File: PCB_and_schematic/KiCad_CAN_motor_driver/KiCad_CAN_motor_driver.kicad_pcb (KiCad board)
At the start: 2 copper layers, 90.4 x 45.2 mm, 67 parts, among them J1 SWDIO, J2 UART, J3 POWER IN 24V, J4 MOTOR OUT, J5 CAN, J6 PWM IN, Q1 BTN8982TA, Q2 BTN8982TA, U1 SN65HVD232, U2 LMR50410, U3 STM32F103C8Tx

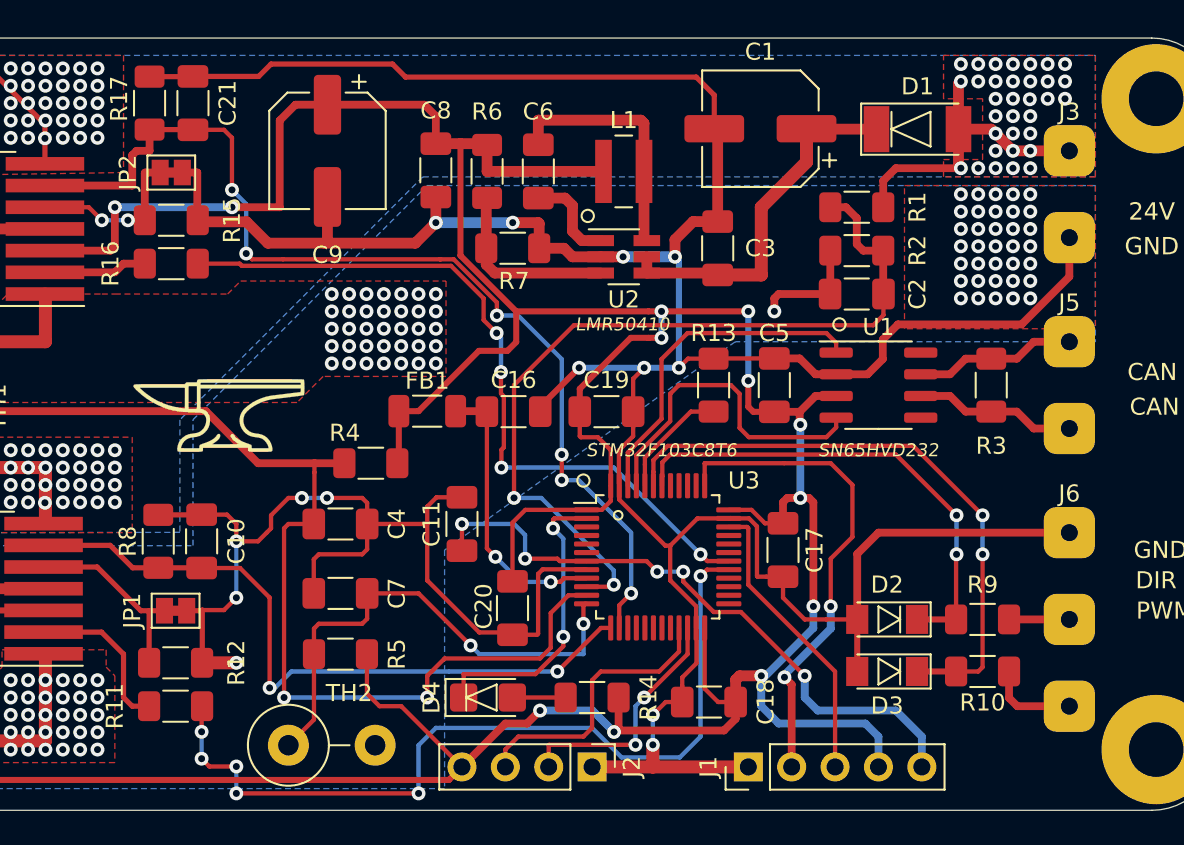
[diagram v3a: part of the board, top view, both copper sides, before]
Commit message: Added JLC PCB ID placeholder,
+traces optimization
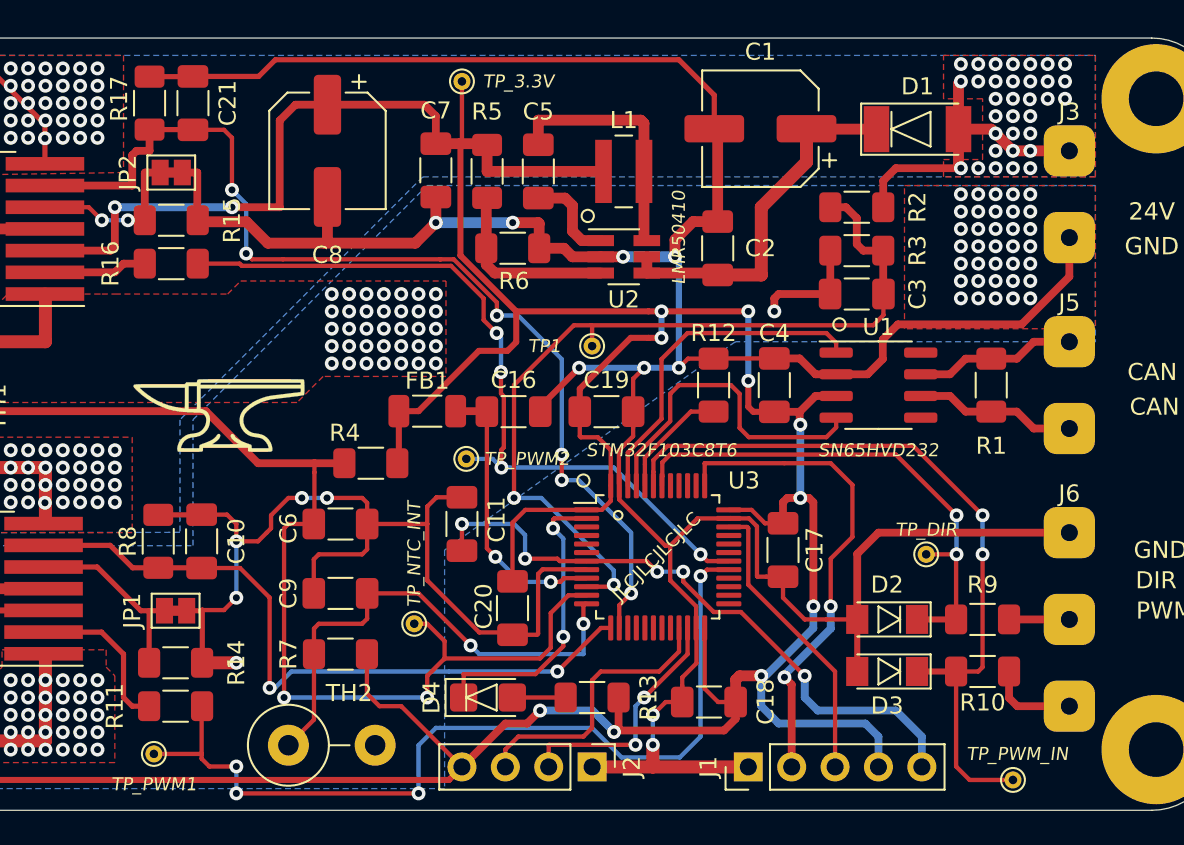
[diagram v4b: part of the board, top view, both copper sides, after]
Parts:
- added TP1: VIN, TestPoint:TestPoint_THTPad_D1.0mm_Drill0.5mm, F.Cu at (159.8, 95.0)
- added TP_3.3V: 3V3, TestPoint:TestPoint_THTPad_D1.0mm_Drill0.5mm, F.Cu at (152.1, 79.5)
- added TP_DIR: DIR, TestPoint:TestPoint_THTPad_D1.0mm_Drill0.5mm, F.Cu at (179.3, 107.2)
- added TP_NTC_INT: NTC INT, TestPoint:TestPoint_THTPad_D1.0mm_Drill0.5mm, F.Cu at (149.4, 111.3)
- added TP_PWM1: PWM OUT 1, TestPoint:TestPoint_THTPad_D1.0mm_Drill0.5mm, F.Cu at (134.1, 118.9)
- added TP_PWM2: PWM OUT 2, TestPoint:TestPoint_THTPad_D1.0mm_Drill0.5mm, F.Cu at (152.4, 101.6)
- added TP_PWM_IN: PWM IN, TestPoint:TestPoint_THTPad_D1.0mm_Drill0.5mm, F.Cu at (184.4, 120.4)
- R10, R9: value 1k -> 6.8k
- renumbered C3 to C2, C2 to C3, C5 to C4, C6 to C5, C4 to C6, C8 to C7, C9 to C8, C7 to C9, R3 to R1, R13 to R12, R14 to R13, R12 to R14, R1 to R2, R2 to R3, R6 to R5, R7 to R6, R5 to R7
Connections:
- U1 pad 5: (no net) -> Net-(U1-Pad5)
- U1 pad 8: (no net) -> Net-(U1-Pad8)
- U3 pad 15: (no net) -> Net-(U3-Pad15)
- U3 pad 16: (no net) -> Net-(U3-Pad16)
- U3 pad 17: (no net) -> Net-(U3-Pad17)
- U3 pad 18: (no net) -> Net-(U3-Pad18)
- U3 pad 19: (no net) -> Net-(U3-Pad19)
- U3 pad 20: (no net) -> Net-(U3-Pad20)
- U3 pad 25: (no net) -> Net-(U3-Pad25)
- U3 pad 26: (no net) -> Net-(U3-Pad26)
- U3 pad 27: (no net) -> Net-(U3-Pad27)
- U3 pad 28: (no net) -> Net-(U3-Pad28)
- U3 pad 3: (no net) -> Net-(U3-Pad3)
- U3 pad 31: (no net) -> Net-(U3-Pad31)
- U3 pad 32: (no net) -> Net-(U3-Pad32)
- U3 pad 33: (no net) -> Net-(U3-Pad33)
- U3 pad 38: (no net) -> Net-(U3-Pad38)
- U3 pad 39: (no net) -> Net-(U3-Pad39)
- U3 pad 4: (no net) -> Net-(U3-Pad4)
- U3 pad 40: (no net) -> Net-(U3-Pad40)
- U3 pad 41: (no net) -> Net-(U3-Pad41)
- U3 pad 5: (no net) -> Net-(U3-Pad5)
- U3 pad 6: (no net) -> Net-(U3-Pad6)
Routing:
- net Net-(D3-Pad1): track 35.6 -> 44.8 mm
- net +3V3: track 234.9 -> 238.6 mm
- net /NTC_INTERNAL: track 60.8 -> 64.0 mm
- net /PWM_1: track 49.7 -> 52.5 mm, vias 6 -> 4
- net /PWM_2: track 43.6 -> 45.9 mm
- net Net-(D2-Pad1): track 28.7 -> 30.4 mm
- net /VIN: track 48.8 -> 50.1 mm
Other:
- board text added: "JLCJLCJLCJLC"

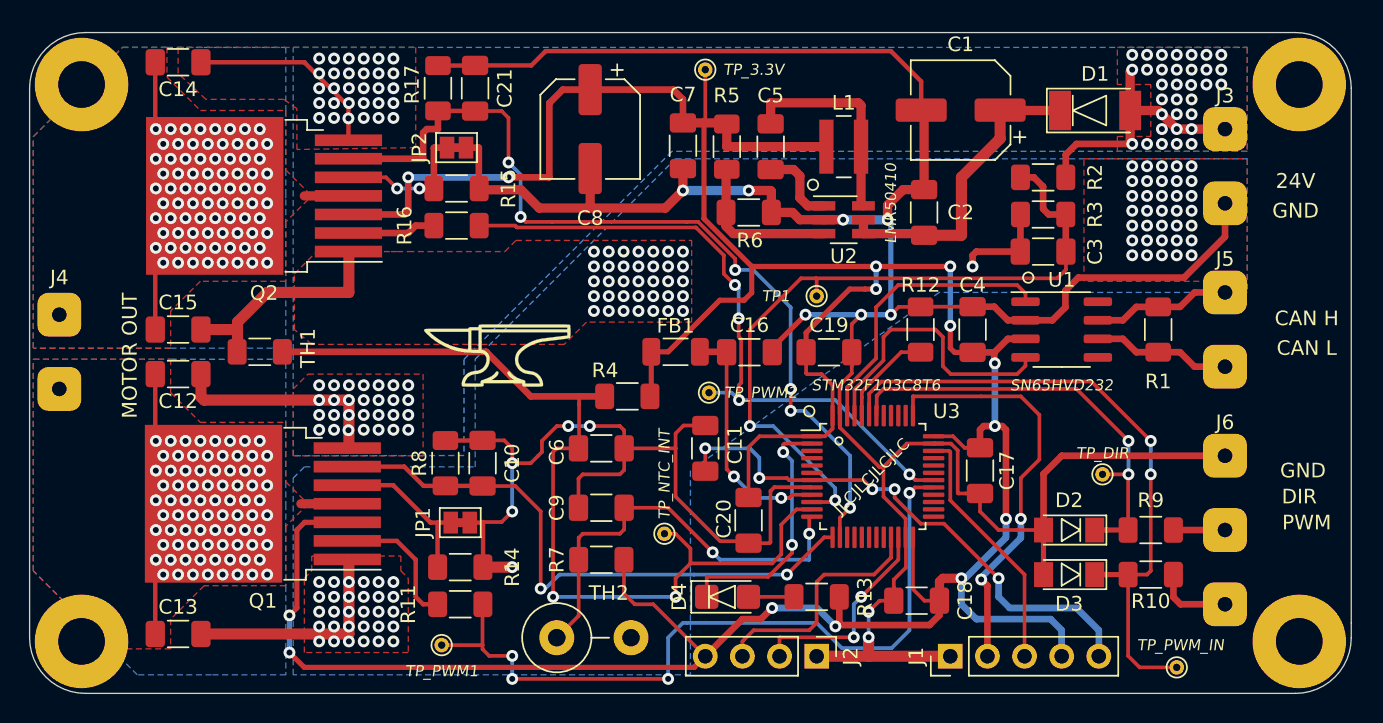
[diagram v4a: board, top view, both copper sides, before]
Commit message: Final PCB version (rev 1.0)
+ reduced amount of vias
+ increased distance between vias
+ removed vias from half-bridge's bottom and moved them closer to motor output pads
+ changed PWM input connector to goldpin
+ added jumper (default open) connecting terminating resistor to CAN bus

+ updated PDF schematic
+updated 3D models
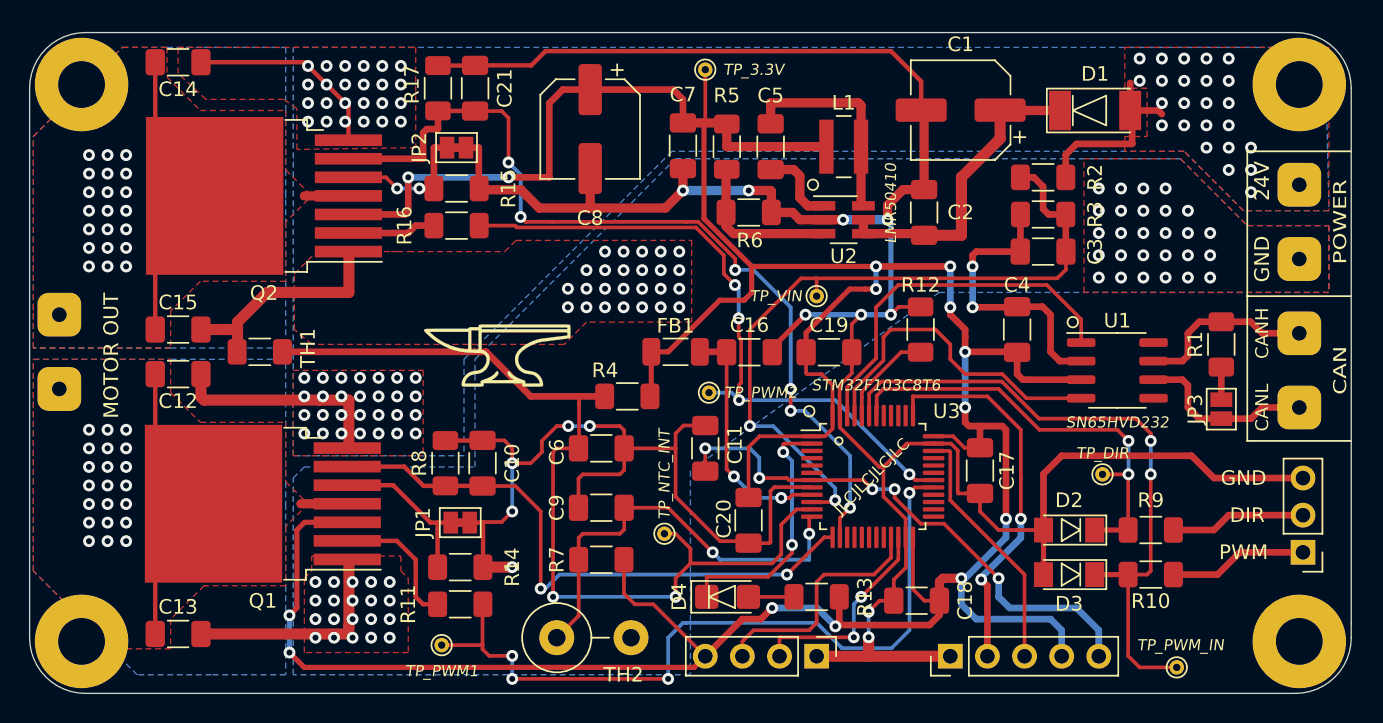
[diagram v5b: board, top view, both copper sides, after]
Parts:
- added JP3: Jumper, Jumper:SolderJumper-2_P1.3mm_Open_Pad1.0x1.5mm, F.Cu at (187.5, 102.7)
- J6: value PWM IN -> PWM_IN; footprint WK_lib:PowerPad_3x_3mm -> Connector_PinHeader_2.54mm:PinHeader_1x03_P2.54mm_Vertical
- moved J6 6.71 mm to (193.0, 112.5), turned to 180 degrees
- moved J3 6.35 mm to (192.8, 89.9)
- moved J5 5.80 mm to (192.8, 100.1)
- moved U1 4.72 mm to (180.3, 100.1)
- moved R1 4.44 mm to (187.5, 98.3)
- moved C4 3.05 mm to (173.5, 97.3)
- renumbered TP1 to TP_VIN
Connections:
- J6 pad 1: GND -> /PWM_IN
- J6 pad 3: /PWM_IN -> GND
- R1 pad 2: /CAN_L -> Net-(JP3-Pad1)
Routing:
- net GND: track 299.4 -> 292.1 mm, vias 115 -> 88
- net /DIR_IN: track 3.53 -> 9.28 mm
- net +24V: track 47.4 -> 41.7 mm, vias 91 -> 76
- net +3V3: track 238.6 -> 244.2 mm
- net /CAN_TX: track 19.9 -> 25.5 mm
- net /PWM_IN: track 5.28 -> 9.50 mm
- net /CAN_RX: track 19.4 -> 22.5 mm
- net /CAN_H: track 9.49 -> 12.3 mm
- net /CAN_L: track 9.49 -> 12.3 mm
- net /SWCLK: track 28.8 -> 26.4 mm
- net Net-(JP3-Pad1): track 0.00 -> 2.23 mm
- net /MOT_B: vias 80 -> 21
- net /MOT_A: vias 80 -> 21
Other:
- board text added: "CAN"
- board text added: "CANH"
- board text added: "CANL"
- board text added: "POWER"
- board text removed: "CAN H"
- board text removed: "CAN L"

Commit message: PCB and schematic rev 1.1
+ revision 1.1 of schematic and PCB
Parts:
- removed the G*** at (169.9, 81.0)
- removed the G*** at (137.9, 99.1)
- removed MountHole (x4): MountingHole_3.2mm_M3_Pad, MountingHole:MountingHole_3.2mm_M3_Pad
- removed REF**: OSHW-Logo2_7.3x6mm_SilkScreen, Symbol:OSHW-Logo2_7.3x6mm_SilkScreen
- removed REF**: KiCad-Logo2_5mm_SilkScreen, Symbol:KiCad-Logo2_5mm_SilkScreen
- removed TP_3.3V: 3V3, TestPoint:TestPoint_THTPad_D1.0mm_Drill0.5mm
- removed TP_DIR: DIR, TestPoint:TestPoint_THTPad_D1.0mm_Drill0.5mm
- removed TP_NTC_INT: NTC INT, TestPoint:TestPoint_THTPad_D1.0mm_Drill0.5mm
- removed TP_PWM1: PWM OUT 1, TestPoint:TestPoint_THTPad_D1.0mm_Drill0.5mm
- removed TP_PWM2: PWM OUT 2, TestPoint:TestPoint_THTPad_D1.0mm_Drill0.5mm
- removed TP_PWM_IN: PWM IN, TestPoint:TestPoint_THTPad_D1.0mm_Drill0.5mm
- removed TP_VIN: VIN, TestPoint:TestPoint_THTPad_D1.0mm_Drill0.5mm
- added C22: 10nF, Capacitor_SMD:C_0805_2012Metric, F.Cu at (177.8, 48.9)
- added C23: 10nF, Capacitor_SMD:C_0805_2012Metric, F.Cu at (191.8, 54.5)
- added C25: 100nF, Capacitor_SMD:C_1206_3216Metric, F.Cu at (168.4, 41.9)
- added D5: LED, LED_SMD:LED_0805_2012Metric_Castellated, F.Cu at (191.3, 61.0)
- added FB2: Ferrite_Bead, Inductor_SMD:L_1206_3216Metric_Pad1.22x1.90mm_HandSolder, F.Cu at (184.4, 41.9)
- added G***: LOGO, WK_lib:Anvil_10x10mm, B.Cu at (193.4, 24.1)
- added R18: 1k, Resistor_SMD:R_0805_2012Metric, F.Cu at (178.6, 58.4)
- added R19: 470R, Resistor_SMD:R_0805_2012Metric, F.Cu at (179.8, 48.9)
- added R20: 33k, Resistor_SMD:R_0805_2012Metric, F.Cu at (189.7, 54.5)
- added TP1: VIN, TestPoint:TestPoint_THTPad_D1.0mm_Drill0.5mm, F.Cu at (209.3, 38.0)
- added TP2: NTC INT, TestPoint:TestPoint_THTPad_D1.0mm_Drill0.5mm, F.Cu at (179.5, 39.8)
- added TP3: 3V3, TestPoint:TestPoint_THTPad_D1.0mm_Drill0.5mm, F.Cu at (187.2, 39.0)
- added TP5: PWM OUT 1, TestPoint:TestPoint_THTPad_D1.0mm_Drill0.5mm, F.Cu at (202.2, 49.3)
- added TP7: PWM OUT 2, TestPoint:TestPoint_THTPad_D1.0mm_Drill0.5mm, F.Cu at (202.2, 47.1)
- C10, C11, C16, C19, C2, C20, C3, C4, C5, C6, C7, C9: footprint Capacitor_SMD:C_1206_3216Metric_Pad1.33x1.80mm_HandSolder -> Capacitor_SMD:C_0805_2012Metric
- C12: value 220nF -> 10nF; footprint Capacitor_SMD:C_1206_3216Metric_Pad1.33x1.80mm_HandSolder -> Capacitor_SMD:C_0805_2012Metric
- C15: value 220nF -> 100nF; footprint Capacitor_SMD:C_1206_3216Metric_Pad1.33x1.80mm_HandSolder -> Capacitor_SMD:C_0805_2012Metric
- C17, C18: value 100nF -> 220nF
- C21: value 10nF -> 100nF; footprint Capacitor_SMD:C_1206_3216Metric_Pad1.33x1.80mm_HandSolder -> Capacitor_SMD:C_0805_2012Metric
- D2: value 3V -> SD24_SOD323; footprint Diode_SMD:D_MiniMELF -> Diode_SMD:D_SOD-323
- D4: value LED -> 3V; footprint LED_SMD:LED_1206_3216Metric_Castellated -> Diode_SMD:D_MiniMELF
- FB1: footprint Inductor_SMD:L_1206_3216Metric_Pad1.22x1.90mm_HandSolder -> Inductor_SMD:L_1206_3216Metric
- J3: value POWER IN 24V -> PWM_IN; footprint WK_lib:PowerPad_2x_3mm -> Connector_PinHeader_2.54mm:PinHeader_1x03_P2.54mm_Vertical
- J4: value MOTOR OUT -> POWER IN 24V; footprint WK_lib:PowerPad_2x_3mm -> WK_lib:ScrewTerminal_2_P5.08mm
- J5: value CAN -> MOTOR OUT; footprint WK_lib:PowerPad_2x_3mm -> WK_lib:ScrewTerminal_2_P5.08mm
- J6: value PWM_IN -> CAN; footprint Connector_PinHeader_2.54mm:PinHeader_1x03_P2.54mm_Vertical -> WK_lib:ScrewTerminal_2_P5.08mm
- JP1: footprint Jumper:SolderJumper-2_P1.3mm_Bridged_Pad1.0x1.5mm -> Jumper:SolderJumper-2_P1.3mm_Open_Pad1.0x1.5mm
- JP3: footprint Jumper:SolderJumper-2_P1.3mm_Open_Pad1.0x1.5mm -> Jumper:SolderJumper-2_P1.3mm_Bridged_Pad1.0x1.5mm
- R1: value 120R -> 10R; footprint Resistor_SMD:R_1206_3216Metric_Pad1.30x1.75mm_HandSolder -> Resistor_SMD:R_0805_2012Metric
- R10, R17, R9: footprint Resistor_SMD:R_1206_3216Metric_Pad1.30x1.75mm_HandSolder -> Resistor_SMD:R_0805_2012Metric
- R11: value 1k -> 33k; footprint Resistor_SMD:R_1206_3216Metric_Pad1.30x1.75mm_HandSolder -> Resistor_SMD:R_0805_2012Metric
- R12: value 10k -> 470R; footprint Resistor_SMD:R_1206_3216Metric_Pad1.30x1.75mm_HandSolder -> Resistor_SMD:R_0805_2012Metric
- R13: value 1.5k -> 10k; footprint Resistor_SMD:R_1206_3216Metric_Pad1.30x1.75mm_HandSolder -> Resistor_SMD:R_0805_2012Metric
- R14: value 470R -> 1.1k; footprint Resistor_SMD:R_1206_3216Metric_Pad1.30x1.75mm_HandSolder -> Resistor_SMD:R_0805_2012Metric
- R15: value 470R -> 1k; footprint Resistor_SMD:R_1206_3216Metric_Pad1.30x1.75mm_HandSolder -> Resistor_SMD:R_0805_2012Metric
- R16: value 1k -> 470R; footprint Resistor_SMD:R_1206_3216Metric_Pad1.30x1.75mm_HandSolder -> Resistor_SMD:R_0805_2012Metric
- R2: value 10k -> 120R; footprint Resistor_SMD:R_1206_3216Metric_Pad1.30x1.75mm_HandSolder -> Resistor_SMD:R_0805_2012Metric
- R3: value 1.1k -> 10k; footprint Resistor_SMD:R_1206_3216Metric_Pad1.30x1.75mm_HandSolder -> Resistor_SMD:R_0805_2012Metric
- R4: value 10k -> 1.1k; footprint Resistor_SMD:R_1206_3216Metric_Pad1.30x1.75mm_HandSolder -> Resistor_SMD:R_0805_2012Metric
- R5: value 51k -> 10k; footprint Resistor_SMD:R_1206_3216Metric_Pad1.30x1.75mm_HandSolder -> Resistor_SMD:R_0805_2012Metric
- R6: value 22k -> 51k; footprint Resistor_SMD:R_1206_3216Metric_Pad1.30x1.75mm_HandSolder -> Resistor_SMD:R_0805_2012Metric
- R7: value 10k -> 22k; footprint Resistor_SMD:R_1206_3216Metric_Pad1.30x1.75mm_HandSolder -> Resistor_SMD:R_0805_2012Metric
- R8: value 470R -> 10k; footprint Resistor_SMD:R_1206_3216Metric_Pad1.30x1.75mm_HandSolder -> Resistor_SMD:R_0805_2012Metric
- TH2: footprint Resistor_THT:R_Axial_DIN0414_L11.9mm_D4.5mm_P5.08mm_Vertical -> Connector_PinHeader_2.54mm:PinHeader_1x02_P2.54mm_Vertical
- moved J4 132.0 mm to (220.2, 29.5)
- moved C13 105.3 mm to (161.4, 23.1), turned to 180 degrees
- moved JP1 102.8 mm to (214.1, 44.3), turned to 270 degrees
- moved C12 97.3 mm to (178.3, 25.5), turned to 0 degrees
- moved R7 93.7 mm to (191.3, 31.5), turned to 90 degrees
- moved Q1 91.2 mm to (167.3, 30.1)
- moved C15 89.5 mm to (186.9, 42.7), turned to 90 degrees
- moved R4 87.3 mm to (206.2, 38.0)
- moved R13 86.2 mm to (194.4, 36.7), turned to 270 degrees
- moved D4 85.4 mm to (210.9, 52.2), turned to 180 degrees
- moved D2 83.6 mm to (202.9, 31.5), turned to 270 degrees
- moved R14 79.9 mm to (192.3, 57.4), turned to 180 degrees
- moved C20 79.7 mm to (190.4, 38.9), turned to 0 degrees
- moved R11 79.5 mm to (185.7, 54.5), turned to 270 degrees
- moved J6 77.4 mm to (220.2, 40.0), turned to 270 degrees
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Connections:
- C12 pad 1: +24V -> Net-(C12-Pad1)
- C12 pad 2: /MOT_A -> GND
- C13 pad 1: /MOT_A -> +24V
- C13 pad 2: GND -> /MOT_A
- C14 pad 1: +24V -> /MOT_A
- C14 pad 2: /MOT_B -> GND
- C15 pad 1: /MOT_B -> Net-(C15-Pad1)
- C16 pad 1: Net-(C16-Pad1) -> +3V3
- C17 pad 1: +3V3 -> +24V
- C17 pad 2: GND -> /MOT_B
- C18 pad 1: +3V3 -> /MOT_B
- C21 pad 1: /I_SENSE_2 -> +3V3
- C4 pad 1: +3V3 -> Net-(C4-Pad1)
- C4 pad 2: GND -> Net-(C4-Pad2)
- C5 pad 1: Net-(C5-Pad1) -> +3V3
- C5 pad 2: Net-(C5-Pad2) -> GND
- C7 pad 1: +3V3 -> Net-(C7-Pad1)
- C8 pad 1: +3V3 -> Net-(C7-Pad1)
- D1 pad 1: Net-(C1-Pad1) -> Net-(D1-Pad1)
- D2 pad 1: Net-(D2-Pad1) -> Net-(C1-Pad1)
- D4 pad 2: Net-(D4-Pad2) -> GND
- FB1 pad 2: Net-(C16-Pad1) -> Net-(C7-Pad1)
- J3 pad 1: GND -> /PWM_IN
- J3 pad 2: +24V -> /DIR_IN
- J4 pad 1: /MOT_B -> +24V
- J4 pad 2: /MOT_A -> GND
- J5 pad 1: /CAN_L -> /MOT_B
- J5 pad 2: /CAN_H -> /MOT_A
- J6 pad 1: /PWM_IN -> /CAN_H
- J6 pad 2: /DIR_IN -> /CAN_L
- JP1 pad 2: GND -> /CAN_L
- JP3 pad 2: /CAN_L -> GND
- L1 pad 1: Net-(C5-Pad2) -> Net-(C4-Pad2)
- L1 pad 2: +3V3 -> Net-(C7-Pad1)
- Q1 pad 5: Net-(JP1-Pad1) -> Net-(JP2-Pad1)
- Q1 pad 6: /I_SENSE_1 -> Net-(C12-Pad1)
- Q2 pad 5: Net-(JP2-Pad1) -> Net-(JP3-Pad1)
- Q2 pad 6: /I_SENSE_2 -> Net-(C22-Pad1)
- R1 pad 1: /CAN_H -> Net-(D1-Pad1)
- R1 pad 2: Net-(JP3-Pad1) -> Net-(C1-Pad1)
- R10 pad 2: Net-(D3-Pad1) -> Net-(D4-Pad1)
- R11 pad 1: /PWM_1 -> /I_SENSE_1
- R11 pad 2: Net-(Q1-Pad2) -> Net-(C12-Pad1)
- R12 pad 1: GND -> Net-(C12-Pad1)
- R12 pad 2: Net-(R12-Pad2) -> GND
- R13 pad 1: +3V3 -> GND
- R13 pad 2: Net-(D4-Pad2) -> Net-(R13-Pad2)
- R14 pad 1: Net-(JP1-Pad1) -> +3V3
- R14 pad 2: GND -> Net-(D5-Pad2)
- R15 pad 1: Net-(JP2-Pad1) -> /PWM_1
- R15 pad 2: GND -> Net-(Q1-Pad2)
- R16 pad 1: Net-(Q2-Pad2) -> Net-(JP2-Pad1)
- R16 pad 2: /PWM_2 -> GND
- R17 pad 1: /I_SENSE_2 -> Net-(JP3-Pad1)
- R2 pad 1: +24V -> /CAN_H
- R2 pad 2: /VIN -> Net-(JP1-Pad1)
- R3 pad 1: /VIN -> +24V
- R3 pad 2: GND -> /VIN
- R4 pad 1: +3V3 -> /VIN
- R4 pad 2: /NTC_INTERNAL -> GND
- R5 pad 2: Net-(R5-Pad2) -> /NTC_INTERNAL
- R6 pad 1: Net-(R5-Pad2) -> Net-(C7-Pad1)
- R6 pad 2: GND -> Net-(R6-Pad2)
- R7 pad 1: +3V3 -> Net-(R6-Pad2)
- R7 pad 2: /NTC_EXTERNAL -> GND
- R8 pad 1: /I_SENSE_1 -> +3V3
- R8 pad 2: GND -> /NTC_EXTERNAL
- R9 pad 2: Net-(D2-Pad1) -> Net-(D3-Pad1)
- U1 pad 5: Net-(U1-Pad5) -> (no net)
- U1 pad 8: Net-(U1-Pad8) -> (no net)
- U2 pad 1: Net-(C5-Pad1) -> Net-(C4-Pad1)
- U2 pad 3: Net-(R5-Pad2) -> Net-(R6-Pad2)
- U2 pad 6: Net-(C5-Pad2) -> Net-(C4-Pad2)
- U3 pad 15: Net-(U3-Pad15) -> (no net)
- U3 pad 16: Net-(U3-Pad16) -> (no net)
- U3 pad 17: Net-(U3-Pad17) -> (no net)
- U3 pad 18: Net-(U3-Pad18) -> (no net)
- U3 pad 19: Net-(U3-Pad19) -> (no net)
- U3 pad 2: Net-(D4-Pad1) -> Net-(D5-Pad1)
- U3 pad 20: Net-(U3-Pad20) -> (no net)
- U3 pad 25: Net-(U3-Pad25) -> (no net)
- U3 pad 26: Net-(U3-Pad26) -> (no net)
- U3 pad 27: Net-(U3-Pad27) -> (no net)
- U3 pad 28: Net-(U3-Pad28) -> (no net)
- U3 pad 3: Net-(U3-Pad3) -> (no net)
- U3 pad 31: Net-(U3-Pad31) -> (no net)
- U3 pad 32: Net-(U3-Pad32) -> (no net)
- U3 pad 33: Net-(U3-Pad33) -> (no net)
- U3 pad 38: Net-(U3-Pad38) -> (no net)
- U3 pad 39: Net-(U3-Pad39) -> (no net)
- U3 pad 4: Net-(U3-Pad4) -> (no net)
- U3 pad 40: Net-(U3-Pad40) -> (no net)
- U3 pad 41: Net-(U3-Pad41) -> (no net)
- U3 pad 42: Net-(D2-Pad1) -> Net-(D3-Pad1)
- U3 pad 43: Net-(D3-Pad1) -> Net-(D4-Pad1)
- U3 pad 44: Net-(R12-Pad2) -> Net-(R13-Pad2)
- U3 pad 5: Net-(U3-Pad5) -> (no net)
- U3 pad 6: Net-(U3-Pad6) -> (no net)
- U3 pad 9: Net-(C16-Pad1) -> Net-(C15-Pad1)
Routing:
- net +3V3: track 244.2 -> 145.8 mm, vias 14 -> 0
- net GND: track 292.1 -> 233.1 mm, vias 88 -> 53
- net /I_SENSE_2: track 61.2 -> 5.71 mm, vias 6 -> 0
- net Net-(C12-Pad1): track 0.00 -> 49.8 mm, vias 0 -> 2
- net Net-(C7-Pad1): track 0.00 -> 36.6 mm
- net /NTC_INTERNAL: track 64.0 -> 28.2 mm
- net /I_SENSE_1: track 41.2 -> 8.90 mm, vias 2 -> 0
- net Net-(D2-Pad1): track 30.4 -> 0.00 mm, vias 2 -> 0
- net Net-(C22-Pad1): track 0.00 -> 26.2 mm, vias 0 -> 2
- net Net-(D5-Pad1): track 0.00 -> 25.9 mm, vias 0 -> 4
- net Net-(C16-Pad1): track 16.8 -> 0.00 mm, vias 2 -> 0
- net /PWM_1: track 52.5 -> 36.8 mm, vias 4 -> 2
- net Net-(C5-Pad2): track 14.6 -> 0.00 mm
- net Net-(D4-Pad1): track 17.5 -> 32.1 mm
- net Net-(C15-Pad1): track 0.00 -> 10.9 mm
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- removed copper zone on B.Cu, net /MOT_A
- removed copper zone on B.Cu, net /MOT_B
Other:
- board size 90.4 x 45.2 mm -> 66.8 x 42.4 mm
- board text added: "CAN H"
- board text added: "CAN L"
- board text added: "EXT TEMP"
- board text added: "NTC EXT"
- board text added: "PWM 1"
- board text added: "PWM 2"
- board text added: "RST"
- board text added: "RX"
- board text added: "Rev 1.1"
- board text added: "TX"
- board text added: "VIN"
- board text removed: "24V"
- board text removed: "CAN"
- board text removed: "CAN HIGH"
- board text removed: "CAN LOW"
- board text removed: "CANH"
- board text removed: "CANL"
- board text removed: "LMR50410"
- board text removed: "POWER"
- board text removed: "Rev 1.0"
- board text removed: "SN65HVD232"
- board text removed: "STM32F103C8T6"

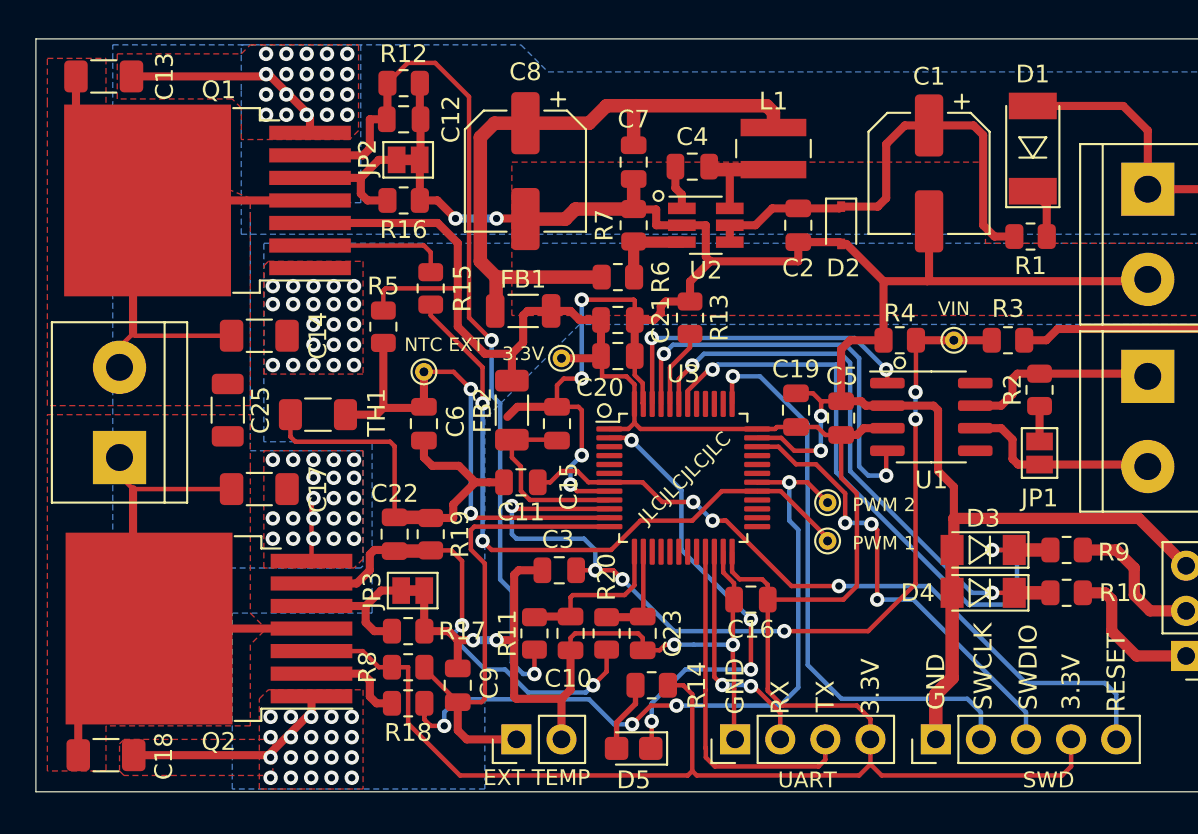
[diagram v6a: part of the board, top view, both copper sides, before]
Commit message: Added back-emf diodes, fixed reading errors
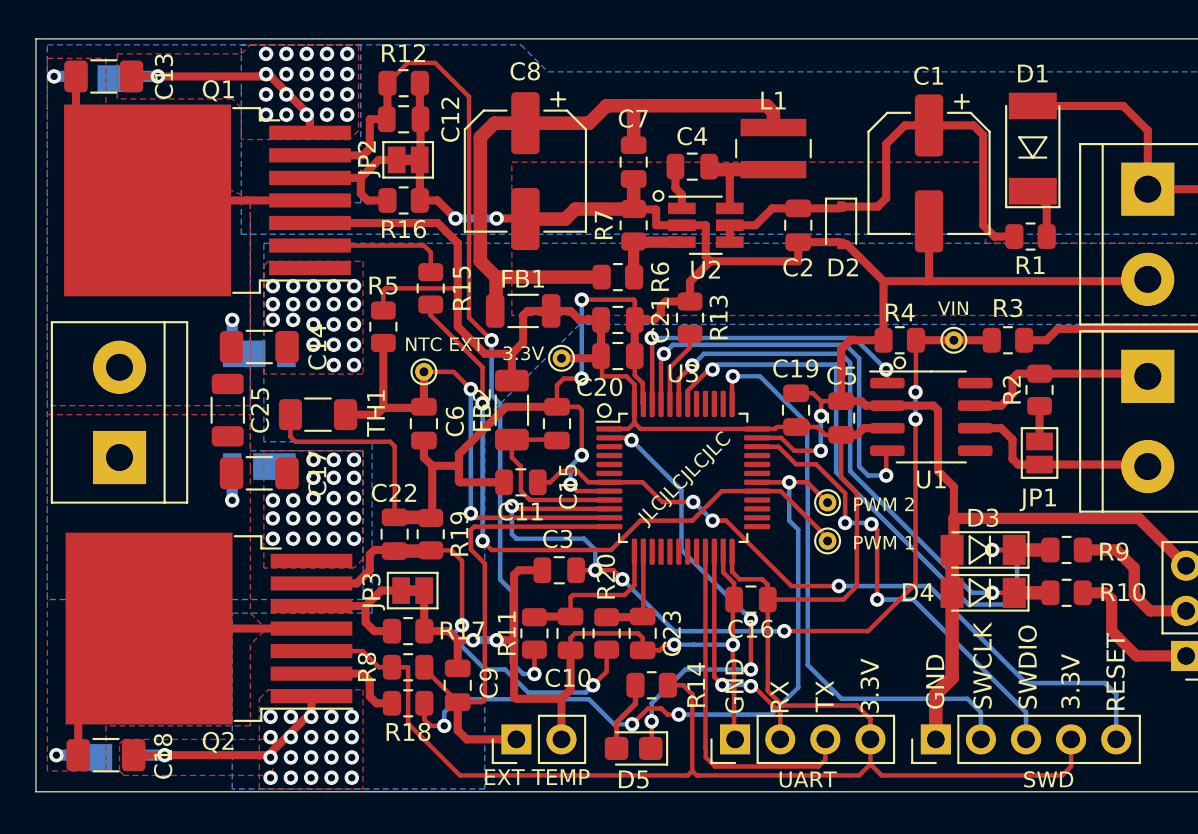
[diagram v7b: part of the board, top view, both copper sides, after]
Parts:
- added D6: D, Diode_SMD:D_PowerDI-123, B.Cu at (161.4, 23.2)
- added D7: D, Diode_SMD:D_PowerDI-123, B.Cu at (170.2, 38.7)
- added D8: D, Diode_SMD:D_PowerDI-123, B.Cu at (170.2, 45.1)
- added D9: D, Diode_SMD:D_PowerDI-123, B.Cu at (161.5, 61.5)
- moved G*** 2.32 mm to (191.1, 24.5)
- moved C17 0.89 mm to (170.2, 45.5)
- moved C14 0.63 mm to (170.2, 38.4)
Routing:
- net /MOT_B: track 33.8 -> 24.2 mm, vias 0 -> 2
- net /MOT_A: track 33.5 -> 24.7 mm, vias 0 -> 2
- net GND: track 233.1 -> 238.8 mm
- net +24V: track 47.2 -> 46.3 mm, vias 41 -> 42
